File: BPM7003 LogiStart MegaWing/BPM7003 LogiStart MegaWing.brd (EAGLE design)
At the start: 72.4 x 67.9 mm, 89 parts, among them J4 AUDIO_JACK_MX295, Q1 MMBTA56, Q2 MMBTA56, Q3 MMBTA56, Q4 MMBTA56, Q5 MMBTA56, U1 ADC088S102CIMT

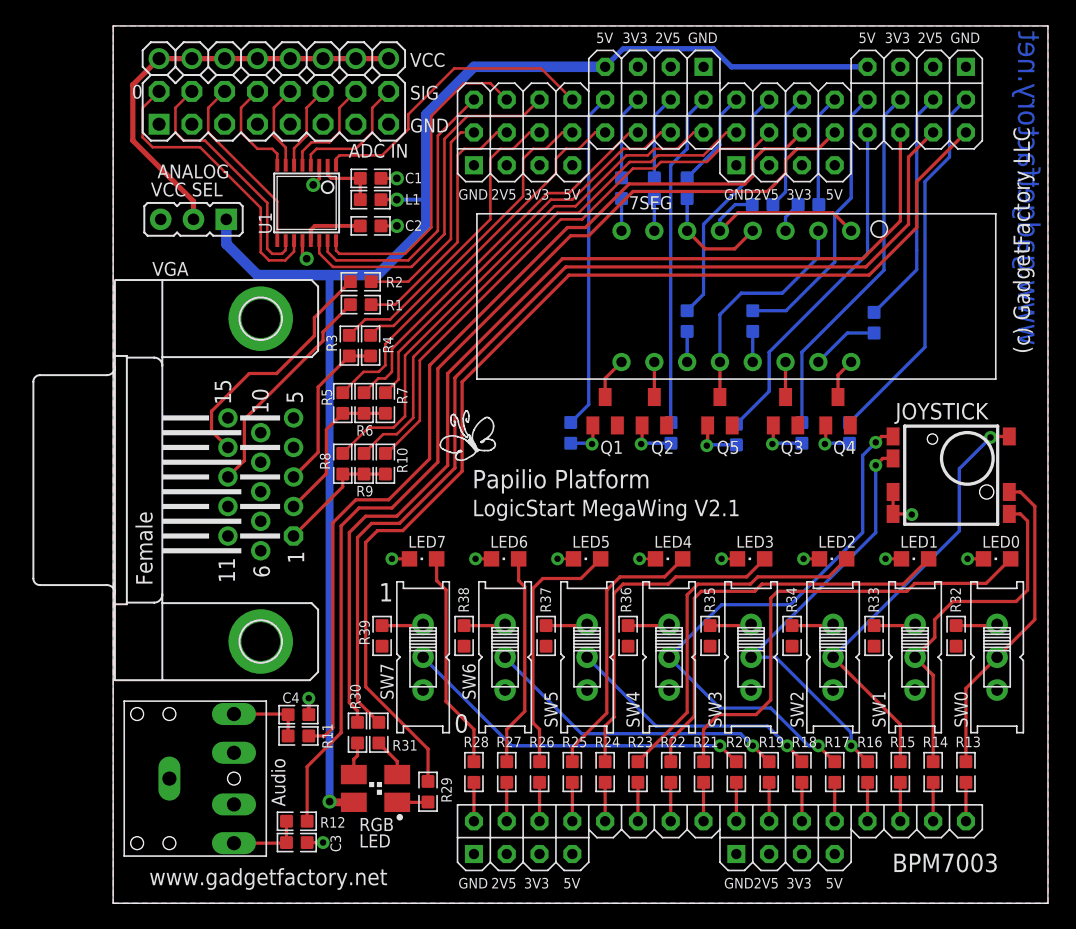
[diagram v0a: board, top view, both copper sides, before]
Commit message: LogicStart MegaWing 2.1.1
Adds buffer to RGB LED.
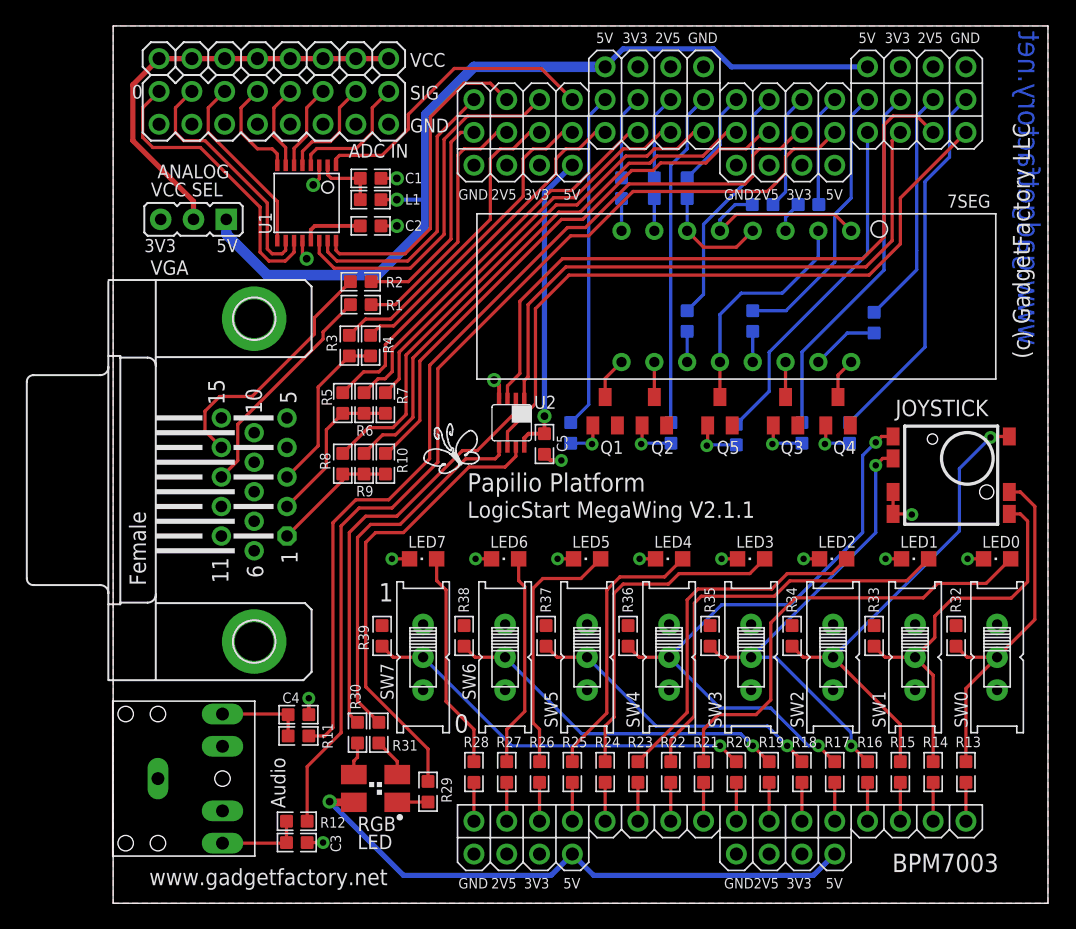
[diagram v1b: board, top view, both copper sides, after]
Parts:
- added C5: 0.1uF, GadgetFactory:0603
- added U2: SN74LVC3G07DCT, GadgetFactory_Pub_1_0:DCT_R-PDSO-G8
- C1, C2: value .1uF -> 0.1uF
- LED8: device GadgetFactory_Pub_1_0:P-LCC-4-3 -> GadgetFactory_Pub_1_0:PLCC4-G
- R1, R2: value 82.5 -> 82.5E
- R10, R7: value 510 -> 499E
- R13, R14, R15, R16, R17, R18, R19, R20: value 4.7K -> 220E
- R21, R22, R23, R24, R25, R26, R27, R28: value 390 -> 390E
- R29: value 330E -> 180E
- R3: value 820 -> 1K
- R30: value 220E -> 300E
- R31: value 220E -> 180E
- R32, R33, R34, R35, R36, R37, R38, R39: value 4.7K -> 10K
- R4: value 390 -> 499E
- R40, R41, R42, R43, R44: value 1K -> 390E
- R46, R47, R48, R49, R50, R51, R52, R53: value 300E -> 220E
- SW0, SW1, SW2, SW3, SW4, SW5, SW6, SW7: device adafruit:EG1218 -> GadgetFactory_Pub_1_0:EG1218
- moved LOGO1 1.63 mm to (26.3, 34.7)
- moved J4 0.89 mm to (5.97, 9.65)
- moved VGA 0.51 mm to (10.9, 32.8)
- turned LED8 to 0 degrees
- turned R32 to 90 degrees
- turned R33 to 90 degrees
- turned R34 to 90 degrees
- turned R35 to 90 degrees
- turned R36 to 90 degrees
- turned R37 to 90 degrees
- turned R38 to 90 degrees
- turned R39 to 90 degrees
- renumbered R45 to R44
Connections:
- net N$10 renamed SEGF
- net N$11 renamed SEGE
- net N$15 renamed SEGDP
- net N$3 renamed SEGB
- net N$5 renamed SEGG
- net N$7 renamed SEGA
- net N$8 renamed SEGD
- net N$9 renamed SEGC
- removed net N$12: LED8.3, R30.2
- removed net N$14: LED8.4, R31.2
- removed net N$16: LED8.1, R29.2
- removed net N$23: R32.1, SW0.O
- removed net N$24: R33.1, SW1.O
- removed net N$33: R34.1, SW2.O
- removed net N$34: R35.1, SW3.O
- removed net N$35: R36.1, SW4.O
- removed net N$36: R37.1, SW5.O
- removed net N$38: R38.1, SW6.O
- removed net N$39: R39.1, SW7.O
- new net LEDB: LED8.3B, R30.2
- new net LEDG: LED8.4G, R31.2
- new net LEDR: LED8.1R, R29.2
- new net RGBB_OUT: R30.1, U2.2
- new net RGBG_OUT: R31.1, U2.5
- new net RGBR_OUT: R29.1, U2.7
- net 5V0: now also C5.1, LED8.2A, U2.8, WING_.W2_5V, WING_.W2_5V_3, WING_.W3_5V, WING_.W3_5V_2; no longer LED8.2
- net GND: now also C5.2, U2.4
- net RGBB: now also U2.6, WING_.A32; no longer R30.1, WING_.A30
- net RGBG: now also U2.3; no longer R31.1
- net RGBR: now also U2.1, WING_.A30; no longer R29.1, WING_.A32
- net SW0_JOY_UP_IN: now also R32.1
- net SW1__JOY_DOWN_IN: now also R33.1
- net SW2_JOY_SELECT_IN: now also R34.1
- net SW3_JOY_RIGHT_IN: now also R35.1
- net SW4_JOY_LEFT_IN: now also R36.1
- net SW5_IN: now also R37.1
- net SW6_IN: now also R38.1
- net SW7_IN: now also R39.1
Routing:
- net RGBR: track 86.3 -> 46.3 mm
- net RGBR_OUT: track 0.00 -> 35.6 mm
- net RGBB_OUT: track 0.00 -> 32.8 mm
- net RGBG_OUT: track 0.00 -> 29.2 mm
- net RGBG: track 79.7 -> 51.5 mm
- net 5V0: track 111.6 -> 138.0 mm, vias 2 -> 3
- net RGBB: track 78.6 -> 52.7 mm
- net SW5_IN: track 20.0 -> 23.6 mm
- net SW7_IN: track 27.6 -> 31.1 mm
- net SW6_IN: track 23.8 -> 27.3 mm
- net SW4_JOY_LEFT_IN: track 44.1 -> 47.6 mm
- net SW3_JOY_RIGHT_IN: track 33.4 -> 36.9 mm
- net SW2_JOY_SELECT_IN: track 33.8 -> 37.3 mm
- net SW0_JOY_UP_IN: track 24.4 -> 27.9 mm
- net SW1__JOY_DOWN_IN: track 27.3 -> 30.6 mm
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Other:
- board text added: "3V3"
- board text added: "5V"
- board text added: "LogicStart MegaWing V2.1.1"
- board text removed: "LogicStart MegaWing V2.1"
